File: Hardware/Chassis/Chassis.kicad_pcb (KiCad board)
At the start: 2 copper layers, 344.8 x 240.3 mm, 6 parts, among them J1 8V, J2 Power relay trigger, J3 Digital In, J5 Digital Out, J6 3.3V (Opt), J8 Relay Power In

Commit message: Measurements of chassis added
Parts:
- moved J3 439.2 mm to (101.3, 222.7)
- moved J5 439.2 mm to (83.7, 79.2)
- moved J8 439.2 mm to (74.3, 221.3)
- moved J1 439.2 mm to (115.9, 81.2)
- moved J2 439.2 mm to (339.4, 81.3)
- moved J6 439.2 mm to (371.7, 81.2)
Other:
- board text added: "230VAC"
- board text added: "Back 4mm"
- board text added: "Front 8mm"
- board text added: "Sides 4mm"

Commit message: Added analog pcb in right position on chassis drawing
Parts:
- added J11: Conn_01x04, Connector_M8:M8 4 pin, F.Cu at (276.7, 359.4)
- added J12: Conn_01x03, Connector_M8:M8 3 pin, F.Cu at (294.1, 359.5)
- added J13: Conn_01x04, Connector_M8:M8 4 pin, F.Cu at (276.7, 389.3)
- added J14: Conn_01x03, Connector_M8:M8 3 pin, F.Cu at (294.2, 389.2)
- added RCA1: RCA_Connector_ALI, RCA ALI:RCA Connector ALI, F.Cu at (121.8, 367.6)
- added RCA10: RCA_Connector_ALI, RCA ALI:RCA Connector ALI, F.Cu at (246.9, 359.3)
- added RCA2: RCA_Connector_ALI, RCA ALI:RCA Connector ALI, F.Cu at (96.3, 367.6)
- added RCA3: RCA_Connector_ALI, RCA ALI:RCA Connector ALI, F.Cu at (70.8, 367.6)
- added RCA4: RCA_Connector_ALI, RCA ALI:RCA Connector ALI, F.Cu at (45.3, 367.6)
- added RCA5: RCA_Connector_ALI, RCA ALI:RCA Connector ALI, F.Cu at (246.9, 389.3)
- added RCA6: RCA_Connector_ALI, RCA ALI:RCA Connector ALI, F.Cu at (121.8, 385.9)
- added RCA7: RCA_Connector_ALI, RCA ALI:RCA Connector ALI, F.Cu at (96.3, 385.9)
- added RCA8: RCA_Connector_ALI, RCA ALI:RCA Connector ALI, F.Cu at (70.8, 385.9)
- added RCA9: RCA_Connector_ALI, RCA ALI:RCA Connector ALI, F.Cu at (45.3, 385.9)
- moved J8 133.6 mm to (44.5, 351.5)
- moved J3 133.6 mm to (71.6, 352.9)
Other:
- board size 344.8 x 240.3 mm -> 362.2 x 370.5 mm
- board text added: "Dette bør være placeret rigtigt"
- board text removed: "A/C in"

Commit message: chassis
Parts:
- moved J11 186.8 mm to (416.2, 483.6)
- moved J13 186.8 mm to (416.2, 513.5)
- moved J14 186.8 mm to (433.7, 513.5)
- moved J3 186.8 mm to (211.1, 477.1)
- moved J8 186.8 mm to (184.1, 475.7)
- moved RCA1 186.8 mm to (261.3, 491.9)
- moved RCA10 186.8 mm to (386.5, 483.6)
- moved RCA2 186.8 mm to (235.8, 491.9)
- moved RCA3 186.8 mm to (210.3, 491.9)
- moved RCA4 186.8 mm to (184.8, 491.9)
- moved J12 186.8 mm to (433.6, 483.7)
- moved RCA5 186.8 mm to (386.5, 513.5)
- moved RCA7 186.8 mm to (235.8, 510.1)
- moved RCA8 186.8 mm to (210.3, 510.1)
- moved RCA9 186.8 mm to (184.8, 510.1)
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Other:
- board size 362.2 x 370.5 mm -> 396.6 x 467.8 mm
- board text added: "12V"

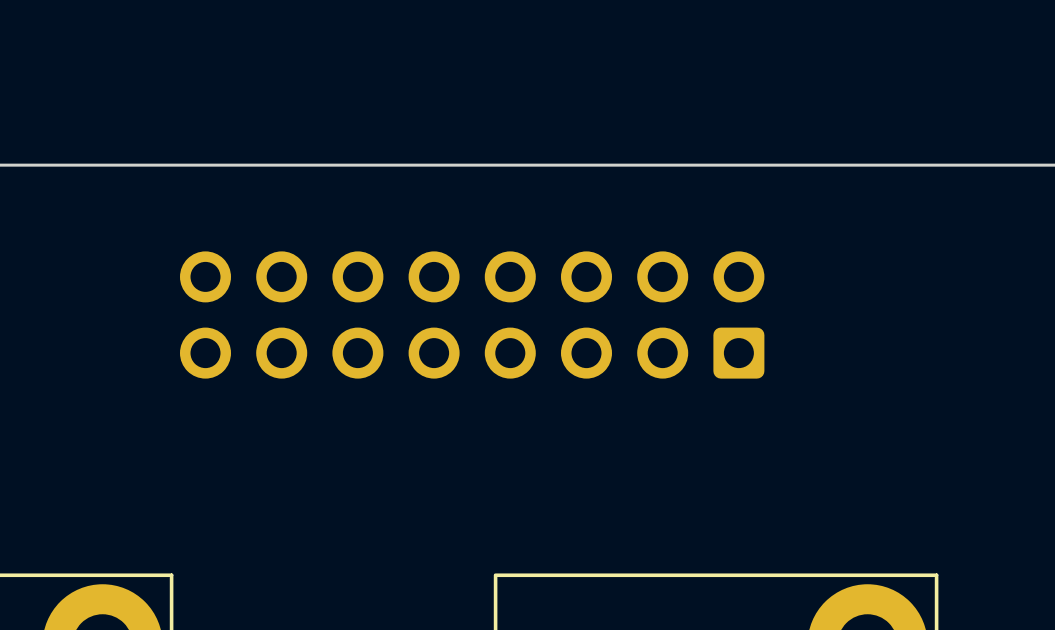
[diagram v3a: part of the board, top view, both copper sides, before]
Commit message: Aligned IDC connector placement between controller and analog pcb
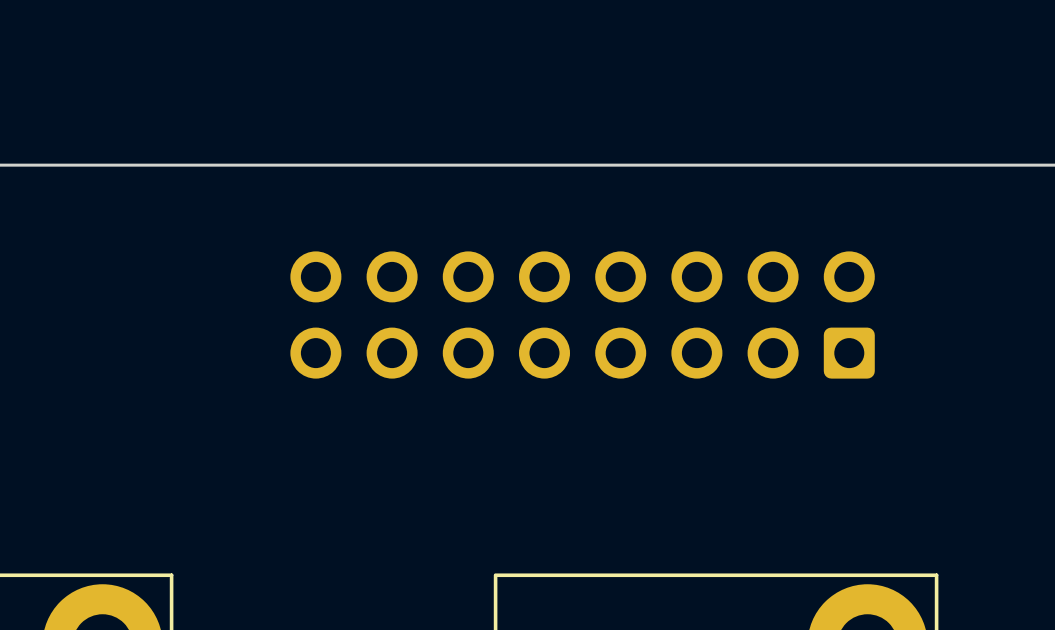
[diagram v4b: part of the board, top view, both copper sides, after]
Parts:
- moved J3 3.68 mm to (214.8, 477.1)
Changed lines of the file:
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@@
 	(net 0 "")
 	(footprint "RCA ALI:RCA Connector ALI"
-		(locked yes)
 		(layer "F.Cu")
 		(at 386.47 483.55)
@@
 	)
 	(footprint "RCA ALI:RCA Connector ALI"
-		(locked yes)
 		(layer "F.Cu")
 		(at 210.33 491.87)
@@
 	)
 	(footprint "RCA ALI:RCA Connector ALI"
-		(locked yes)
 		(layer "F.Cu")
 		(at 210.33 510.07)
@@
 	)
 	(footprint "Connector_M8:M8 3 pin"
-		(locked yes)
 		(layer "F.Cu")
 		(at 433.72 513.46 180)
@@
 	)
 	(footprint "RCA ALI:RCA Connector ALI"
-		(locked yes)
 		(layer "F.Cu")
 		(at 261.33 510.07)
@@
 	)
 	(footprint "RCA ALI:RCA Connector ALI"
-		(locked yes)
 		(layer "F.Cu")
 		(at 386.47 513.55)
@@
 	)
 	(footprint "RCA ALI:RCA Connector ALI"
-		(locked yes)
 		(layer "F.Cu")
 		(at 235.83 491.87)
@@
 	)
 	(footprint "RCA ALI:RCA Connector ALI"
-		(locked yes)
 		(layer "F.Cu")
 		(at 184.83 510.07)
@@
 	)
 	(footprint "RCA ALI:RCA Connector ALI"
-		(locked yes)
 		(layer "F.Cu")
 		(at 184.83 491.87)
@@
 	)
 	(footprint "RCA ALI:RCA Connector ALI"
-		(locked yes)
 		(layer "F.Cu")
 		(at 235.83 510.07)
@@
 	)
 	(footprint "RCA ALI:RCA Connector ALI"
-		(locked yes)
 		(layer "F.Cu")
 		(at 261.33 491.87)
@@
 	)
 	(footprint "Connector_M8:M8 4 pin"
-		(locked yes)
 		(layer "F.Cu")
 		(at 416.25 513.5 180)
@@
 	)
 	(footprint "Connector_M8:M8 3 pin"
-		(locked yes)
 		(layer "F.Cu")
 		(at 433.62 483.7 180)
@@
 	)
 	(footprint "Connector_M8:M8 4 pin"
-		(locked yes)
 		(layer "F.Cu")
 		(at 416.24 483.62 180)
@@
 	)
 	(footprint "Connector_IDC:IDC-Header_2x08_P2.54mm_Vertical"
-		(locked yes)
 		(layer "B.Cu")
-		(at 211.09 477.115 90)
+		(at 214.77 477.115 90)
 		(descr "Through hole IDC box header, 2x08, 2.54mm pitch, DIN 41651 / IEC 60603-13, double rows, https://docs.google.com/spreadsheets/d/16SsEcesNF15N3Lb4niX7dcUr-NY5_MFPQhobNuNppn4/edit#gid=0")
 		(tags "Through hole vertical IDC box header THT 2x08 2.54mm double row")
@@
 	)
 	(footprint "THEPREAMP_POWER_CON:TBP01R2-508-02BK (VERT)"
-		(locked yes)
 		(layer "B.Cu")
 		(at 184.08 475.72 180)
@@
 		(start 157.89 470.85)
 		(end 442.89 535.85)
-		(locked yes)
 		(stroke
 			(width 0.1)
@@
 	)
 	(gr_text "Dette bør være placeret rigtigt"
-		(locked yes)
 		(at 277.92 501.14 0)
 		(layer "Dwgs.User")
@@
 	)
 	(group ""
-		(locked yes)
 		(members "0178d9a1-0823-4960-91fd-b7f50fbc3147" "0b244f52-7bcf-4ebc-bae0-528af5242794"
 			"33caed7f-2eb6-415f-9425-ff5afa25cfb2" "393d9ae8-6dc5-450a-b7bb-8013b3757848"

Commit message: Pcb dimensions
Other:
- board size 396.6 x 467.8 mm -> 393.5 x 467.8 mm
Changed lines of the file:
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@@
-		(layer "Dwgs.User")
-	)
-	(gr_rect
-		(start 508.03 226.165)
-		(end 520.12 232.495)
-		(stroke
-			(width 0.1)
-			(type default)
-		)
-		(fill none)
 		(layer "Dwgs.User")
 	)
@@
 	)
 	(gr_rect
+		(start 401.73 213.375)
+		(end 489.12 454.825)
+		(stroke
+			(width 0.05)
+			(type default)
+		)
+		(fill none)
+		(layer "Edge.Cuts")
+	)
+	(gr_rect
+		(start 309.94 148.7)
+		(end 551.39 236.09)
+		(stroke
+			(width 0.05)
+			(type default)
+		)
+		(fill none)
+		(layer "Edge.Cuts")
+	)
+	(gr_rect
+		(start 310.63 213.775)
+		(end 398.02 455.225)
+		(stroke
+			(width 0.05)
+			(type default)
+		)
+		(fill none)
+		(layer "Edge.Cuts")
+	)
+	(gr_rect
 		(start 157.89 470.85)
 		(end 442.89 535.85)
 		(stroke
 			(width 0.1)
-			(type default)
-		)
-		(fill none)
-		(layer "Edge.Cuts")
-	)
-	(gr_rect
-		(start 480.06 226.115)
-		(end 554.5 327.885)
-		(stroke
-			(width 0.05)
 			(type default)
 		)
@@
 			)
 		)
-	)
-	(zone
-		(net 0)
-		(net_name "")
-		(layer "Dwgs.User")
-		(hatch full 2)
-		(connect_pads
-			(clearance 0)
-		)
-		(min_thickness 0.25)
-		(filled_areas_thickness no)
-		(keepout
-			(tracks not_allowed)
-			(vias not_allowed)
-			(pads not_allowed)
-			(copperpour allowed)
-			(footprints allowed)
-		)
-		(fill
-			(thermal_gap 0.5)
-			(thermal_bridge_width 0.5)
-		)
-		(polygon
-			(pts
-				(xy 507.39 115.72) (xy 508.03 226.165) (xy 520.12 226.165) (xy 520.39 115.72)
-			)
-		)

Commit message: Chassis placement new draft
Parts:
- removed J1: 8V, THE_PREAMP_CONN_POWER_5_08:TBP01R2-508-02BK (VERT)
- removed the J2 at (453.0, 108.2)
- removed the J5 at (197.2, 106.1)
- removed the J6 at (485.3, 108.2)
- removed J8: Relay Power In, THEPREAMP_POWER_CON:TBP01R2-508-02BK (VERT)
- added ?: , , F.Cu at (464.4, 116.0)
- added ?: , , F.Cu at (357.4, 116.0)
- added ?: , , F.Cu at (464.4, 82.0)
- added ?: , , F.Cu at (357.4, 82.0)
- added ?: , , F.Cu at (250.4, 82.0)
- added J2: Power relay trigger, THE_PREAMP_CONN_POWER_5_08:TBP01R2-508-02BK (VERT), B.Cu at (482.9, 151.6)
- added J2: Power relay trigger, THE_PREAMP_CONN_POWER_5_08:TBP01R2-508-02BK (VERT), B.Cu at (483.4, 115.9)
- added J4: 15V AC, THE_PREAMP_CONN_POWER_5_08:TBP01R1-508-02BK, F.Cu at (396.8, 193.6)
- added J4: 15V AC, THE_PREAMP_CONN_POWER_5_08:TBP01R1-508-02BK, F.Cu at (396.2, 301.0)
- added J4: 15V AC, THE_PREAMP_CONN_POWER_5_08:TBP01R1-508-02BK, F.Cu at (375.5, 188.5)
- added J4: 15V AC, THE_PREAMP_CONN_POWER_5_08:TBP01R1-508-02BK, F.Cu at (396.0, 263.7)
- added J5: 230V AC fixed, THE_PREAMP_CONN_POWER_5_08:TBP01R1-508-02BK, F.Cu at (481.3, 194.1)
- added J5: Digital Out, Connector_IDC:IDC-Header_2x08_P2.54mm_Vertical, F.Cu at (162.3, 117.0)
- added J5: 230V AC, THE_PREAMP_CONN_POWER_5_08:TBP01R1-508-02BK, F.Cu at (458.3, 188.5)
- added J5: 230V AC triggered, THE_PREAMP_CONN_POWER_5_08:TBP01R1-508-02BK, F.Cu at (500.5, 226.3)
- added J5: 230V AC, THE_PREAMP_CONN_POWER_5_08:TBP01R1-508-02BK, F.Cu at (542.4, 225.8)
- added J5: 230V AC triggered, THE_PREAMP_CONN_POWER_5_08:TBP01R1-508-02BK, F.Cu at (485.1, 226.1)
- added J5: 230V AC, THE_PREAMP_CONN_POWER_5_08:TBP01R1-508-02BK, F.Cu at (457.6, 277.2)
- added J6: 3.3V (Opt), THE_PREAMP_CONN_POWER_5_08:TBP01R2-508-02BK (VERT), B.Cu at (255.4, 115.0)
- added J6: 3.3V (Opt), THE_PREAMP_CONN_POWER_5_08:TBP01R2-508-02BK (VERT), B.Cu at (230.6, 115.0)
- added J6: 3.3V (Opt), THE_PREAMP_CONN_POWER_5_08:TBP01R2-508-02BK (VERT), B.Cu at (243.0, 115.0)
- added J6: 3.3V (Opt), THE_PREAMP_CONN_POWER_5_08:TBP01R2-508-02BK (VERT), B.Cu at (243.1, 152.6)
- added J6: 3.3V (Opt), THE_PREAMP_CONN_POWER_5_08:TBP01R2-508-02BK (VERT), B.Cu at (230.6, 152.6)
- added J6: 3.3V (Opt), THE_PREAMP_CONN_POWER_5_08:TBP01R2-508-02BK (VERT), B.Cu at (255.5, 152.6)
- moved J3 33.5 mm to (181.3, 477.3)
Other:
- board size 393.5 x 467.8 mm -> 672.9 x 459.3 mm
- board text added: "12V, 8V, 3.3V"
- board text added: "AC trigger"
- board text added: "AC trigger board"
- board text added: "Daughter board"
- board text added: "Hahn trafo"
- board text added: "I2C, SPI, 3.3V, 12V, DGND"
- board text added: "Iron Pre"
- board text added: "Max. dimensions"
- board text added: "Optional"
- board text added: "Right dimensions"
- board text added: "Salas L-adapter 12V + 8V + 3.3V"
- board text added: "Salas SSLV1.1"
- board text added: "or another type"
- board text removed: "12V"
- board text removed: "Dette bør være placeret rigtigt"

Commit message: Chassis placement draft
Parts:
- removed the J4 at (375.5, 188.5)
- removed the J6 at (243.1, 152.6)
- removed the J6 at (230.6, 152.6)
- removed the J6 at (255.5, 152.6)
- added J1: AC in, THE_PREAMP_CONN_POWER_5_08:TBP01R1-508-02BK, F.Cu at (373.6, 188.5)
- added J2: Relay power, THE_PREAMP_CONN_POWER_5_08:TBP01R1-508-02BK, F.Cu at (266.5, 221.1)
- added J6: 8V, THE_PREAMP_CONN_POWER_5_08:TBP01R1-508-02BK, F.Cu at (228.6, 158.3)
- added J7: Opt. 3V3, THE_PREAMP_CONN_POWER_5_08:TBP01R1-508-02BK, F.Cu at (241.2, 158.3)
- added J8: DC in, THE_PREAMP_CONN_POWER_5_08:TBP01R1-508-02BK, F.Cu at (245.5, 216.1)
- added J9: 12V, THE_PREAMP_CONN_POWER_5_08:TBP01R1-508-02BK, F.Cu at (216.0, 158.3)
- moved J6 14.5 mm to (216.1, 115.7)
- moved J6 14.5 mm to (241.0, 115.7)
- moved J6 14.5 mm to (228.6, 115.7)
- moved J5 4.05 mm to (500.5, 222.3)
- moved J5 4.05 mm to (485.1, 222.1)
- moved J5 3.73 mm to (542.4, 222.0)
- moved J4 2.16 mm to (396.8, 261.7)
- moved J4 2.16 mm to (397.0, 299.0)
- moved J5 2.16 mm to (458.4, 275.2)
- moved J2 0.72 mm to (482.7, 152.3)
- moved J5 0.40 mm to (481.0, 193.8)
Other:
- board size 672.9 x 459.3 mm -> 335.9 x 459.3 mm
- board text added: "AC trigger out"
- board text added: "Salas L-adapter"
- board text removed: "AC trigger"
- board text removed: "Iron Pre"
- board text removed: "Salas L-adapter 12V + 8V + 3.3V"

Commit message: Small adjustments to draft
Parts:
- J6: value 8V -> ESP32 power
- J7: value Opt. 3V3 -> Opt. 3V3 power
- J9: value 12V -> Relay power
- moved J1 2.68 mm to (376.1, 187.6)
- moved J8 2.23 mm to (247.8, 216.0)
- moved J2 2.23 mm to (268.7, 221.0)
- moved J5 1.06 mm to (481.0, 192.7)
- moved J5 0.93 mm to (458.6, 187.7)
- moved J4 0.88 mm to (396.7, 192.7)
- moved J2 0.51 mm to (483.2, 152.2)
- moved J6 0.06 mm to (228.6, 158.3)
- moved J7 0.06 mm to (241.2, 158.3)
- moved J9 0.06 mm to (216.0, 158.3)
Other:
- outline, holes or cut-outs redrawn
